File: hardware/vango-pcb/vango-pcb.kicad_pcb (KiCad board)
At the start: 2 copper layers, 70 x 66 mm, 13 parts, among them J1 XT60PW-M, J2 NeoPixel, J3 I2C, J4 Conn_01x07, J5 SPI, J6 Conn_01x02, SW1 SW_SPDT, U1 MD41B, U2 REG15D, U3 MD41B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

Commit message: update kicad pcb
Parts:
- moved SW1 10.9 mm to (94.7, 114.9)
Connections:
- J1 pad 1: Net-(J1-+) -> Net-(J1--)
- J1 pad 2: Net-(J1--) -> Net-(J1-+)
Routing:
- net Net-(J1-+): track 18.4 -> 8.88 mm, vias 1 -> 0
- net Net-(SW1-B): track 11.2 -> 17.2 mm, vias 0 -> 1
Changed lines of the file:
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@@
     (pad "" thru_hole rect (at 10.35 -6 270) (size 0.9 2) (drill oval 0.6 1.7) (layers "*.Cu" "*.Mask"))
     (pad "1" thru_hole roundrect (at 0 0 270) (size 4.1 4.1) (drill 2.7) (layers "*.Cu" "*.Mask") (roundrect_rratio 0.25)
-      (net 49 "Net-(J1-+)") (pinfunction "+") (pintype "passive"))
+      (net 41 "Net-(J1--)") (pinfunction "+") (pintype "passive"))
     (pad "2" thru_hole circle (at 7.2 0 270) (size 4.1 4.1) (drill 2.7) (layers "*.Cu" "*.Mask")
-      (net 41 "Net-(J1--)") (pinfunction "-") (pintype "passive"))
+      (net 49 "Net-(J1-+)") (pinfunction "-") (pintype "passive"))
     (pad "3" thru_hole rect (at 3.6 -3.65 270) (size 2.3 1.3) (drill oval 2 1) (layers "*.Cu" "*.Mask"))
     (model "${KICAD6_3DMODEL_DIR}/Connector_AMASS.3dshapes/AMASS_XT60IPW-M_1x03_P7.20mm_Horizontal.wrl"
@@
   )
   (footprint "Connector_PinHeader_2.54mm:PinHeader_1x03_P2.54mm_Vertical" (layer "F.Cu")
-    (at 83.82 114.3 90)
+    (at 94.662514 114.903264 90)
     (descr "Through hole straight pin header, 1x03, 2.54mm pitch, single row")
     (tags "Through hole pin header THT 1x03 2.54mm single row")
@@
   (segment (start 85.752474 76.807526) (end 83.82 78.74) (width 0.25) (layer "F.Cu") (net 35))
   (segment (start 97.127526 76.807526) (end 85.752474 76.807526) (width 0.25) (layer "F.Cu") (net 35))
-  (segment (start 86.36 114.3) (end 88.9 111.76) (width 0.25) (layer "B.Cu") (net 40))
-  (segment (start 88.9 106.68) (end 86.36 106.68) (width 0.25) (layer "B.Cu") (net 40))
-  (segment (start 88.9 111.76) (end 88.9 106.68) (width 0.25) (layer "B.Cu") (net 40))
+  (segment (start 86.36 106.68) (end 91.44 106.68) (width 0.25) (layer "F.Cu") (net 40))
+  (via (at 91.44 106.68) (size 0.8) (drill 0.4) (layers "F.Cu" "B.Cu") (net 40))
+  (segment (start 91.44 106.68) (end 91.44 111.76) (width 0.25) (layer "B.Cu") (net 40))
+  (segment (start 94.05925 111.76) (end 97.202514 114.903264) (width 0.25) (layer "B.Cu") (net 40))
+  (segment (start 91.44 111.76) (end 94.05925 111.76) (width 0.25) (layer "B.Cu") (net 40))
   (segment (start 92 104.14) (end 86.36 104.14) (width 0.25) (layer "F.Cu") (net 41))
-  (segment (start 95.6 107.74) (end 92 104.14) (width 0.25) (layer "F.Cu") (net 41))
+  (segment (start 95.6 100.54) (end 92 104.14) (width 0.25) (layer "F.Cu") (net 41))
   (segment (start 93.98 71.12) (end 99.06 71.12) (width 0.25) (layer "F.Cu") (net 44))
   (segment (start 81.28 63.5) (end 93.98 63.5) (width 0.25) (layer "F.Cu") (net 44))
@@
   (segment (start 86.36 55.88) (end 83.82 58.42) (width 0.25) (layer "F.Cu") (net 45))
   (segment (start 96.52 55.88) (end 86.36 55.88) (width 0.25) (layer "F.Cu") (net 45))
-  (segment (start 95.6 100.54) (end 92.5 100.54) (width 0.25) (layer "F.Cu") (net 49))
-  (segment (start 92.5 100.54) (end 91.44 101.6) (width 0.25) (layer "F.Cu") (net 49))
-  (via (at 91.44 101.6) (size 0.8) (drill 0.4) (layers "F.Cu" "B.Cu") (net 49))
-  (segment (start 91.44 111.76) (end 88.9 114.3) (width 0.25) (layer "B.Cu") (net 49))
-  (segment (start 91.44 101.6) (end 91.44 111.76) (width 0.25) (layer "B.Cu") (net 49))
+  (segment (start 95.6 110.76075) (end 99.742514 114.903264) (width 0.25) (layer "B.Cu") (net 49))
+  (segment (start 95.6 107.74) (end 95.6 110.76075) (width 0.25) (layer "B.Cu") (net 49))
   (zone (net 4) (net_name "GND") (layer "B.Cu") (hatch edge 0.5)
     (connect_pads (clearance 0.5))

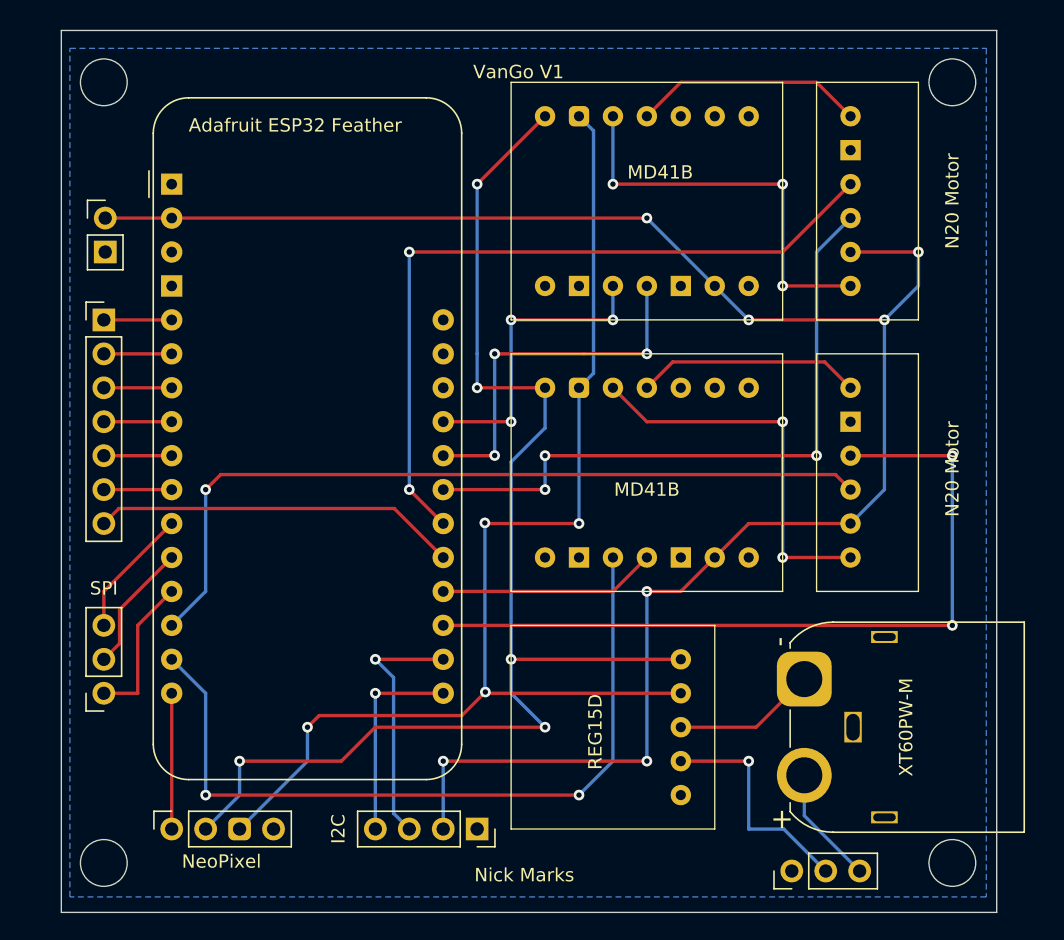
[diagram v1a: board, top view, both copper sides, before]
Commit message: add servo connector, more space for voltage reg
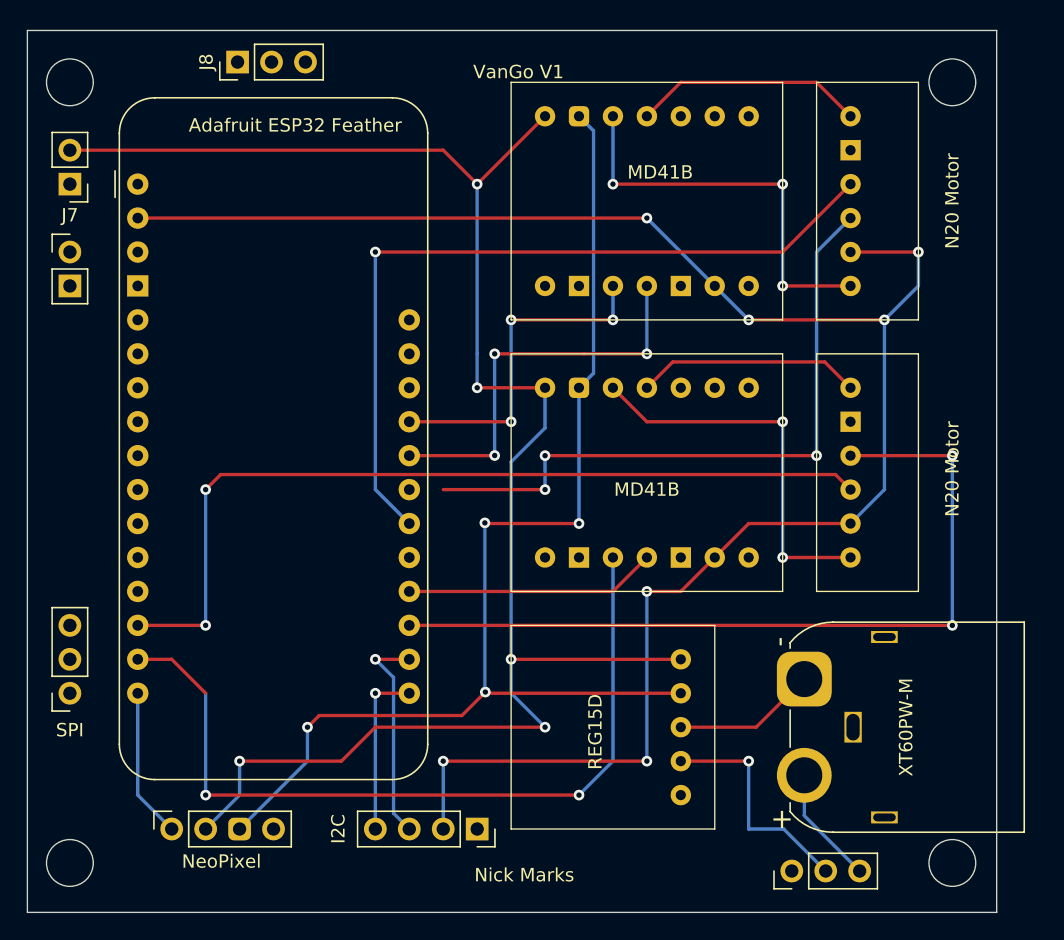
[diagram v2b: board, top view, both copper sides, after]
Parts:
- removed J4: Conn_01x07, Connector_PinHeader_2.54mm:PinHeader_1x07_P2.54mm_Vertical
- added J7: Conn_01x02, Connector_PinHeader_2.54mm:PinHeader_1x02_P2.54mm_Vertical, F.Cu at (40.6, 63.5)
- added J8: Servo, Connector_PinHeader_2.54mm:PinHeader_1x03_P2.54mm_Vertical, F.Cu at (53.2, 54.4)
- moved J6 3.67 mm to (40.6, 68.6)
- moved A1 2.54 mm to (45.7, 63.5)
- moved J5 2.54 mm to (40.6, 101.6)
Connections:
- J1 pad 1: Net-(J1--) -> Net-(J1-+)
- J1 pad 2: Net-(J1-+) -> Net-(J1--)
- J2 pad 3: GNDPWR -> GND
- U1 pad 9: GNDPWR -> GND
- U2 pad 4: GNDPWR -> GND
- U3 pad 9: GNDPWR -> GND
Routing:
- net GNDPWR: track 89.9 -> 0.00 mm, vias 4 -> 0
- net GND: track 0.00 -> 89.9 mm, vias 0 -> 4
- net +5V: track 97.8 -> 129.3 mm
- net /A8: track 27.4 -> 0.00 mm
- net /MISO: track 11.2 -> 0.00 mm
- net /MOSI: track 9.72 -> 0.00 mm
- net /SCK: track 9.72 -> 0.00 mm
- net /A5: track 5.08 -> 0.00 mm
- net /A4: track 5.08 -> 0.00 mm
- net /A3: track 5.08 -> 0.00 mm
- net /A2: track 5.08 -> 0.00 mm
- net /A1: track 5.08 -> 0.00 mm
- net /A0: track 5.08 -> 0.00 mm
- net /IO16: track 60.4 -> 64.4 mm, vias 1 -> 2
- net /IO33: track 56.5 -> 59.0 mm, vias 2 -> 1
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- removed copper zone on B.Cu, net GND
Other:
- board size 70 x 66 mm -> 72.5 x 66 mm

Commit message: pcb should be all good now
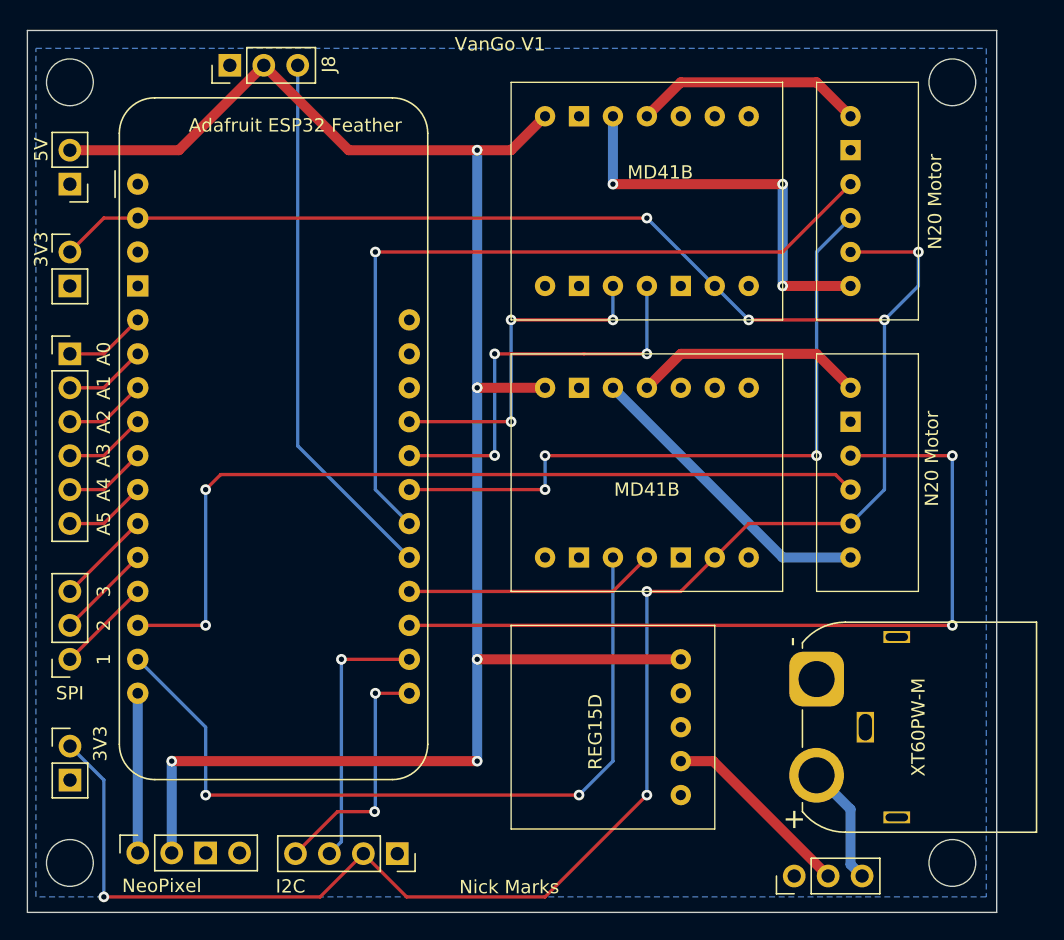
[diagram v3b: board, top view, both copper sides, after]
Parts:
- added 3V3: Conn_01x02, Connector_PinHeader_2.54mm:PinHeader_1x02_P2.54mm_Vertical, F.Cu at (40.7, 105.6)
- added J4: Conn_01x06, Connector_PinHeader_2.54mm:PinHeader_1x06_P2.54mm_Vertical, F.Cu at (40.6, 76.2)
- J8: value Servo -> SG90_Servo
- moved J3 6.25 mm to (65.1, 113.6)
- moved J2 3.11 mm to (45.7, 113.6)
- moved J5 2.54 mm to (40.6, 99.1)
- moved J1 0.92 mm to (96.5, 100.5)
- moved J8 0.63 mm to (52.6, 54.6)
- moved SW1 0.42 mm to (94.8, 115.3)
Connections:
- J1 pad 1: Net-(J1-+) -> GND
- J1 pad 2: Net-(J1--) -> Net-(J1-+)
- U2 pad 3: Net-(J1--) -> GND
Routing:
- net GND: track 89.9 -> 0.00 mm, vias 4 -> 0
- net +3V3: track 136.9 -> 184.1 mm
- net /A8: track 0.00 -> 40.3 mm
- net Net-(J1--): track 10.7 -> 0.00 mm
- net +5V: track 129.3 -> 137.6 mm
- net /SCK: track 0.00 -> 7.18 mm
- net /MOSI: track 0.00 -> 7.18 mm
- net /MISO: track 0.00 -> 7.18 mm
- net /A5: track 0.00 -> 6.13 mm
- net /A4: track 0.00 -> 6.13 mm
- net /A2: track 0.00 -> 6.13 mm
- net /A0: track 0.00 -> 6.13 mm
- net /A3: track 0.00 -> 6.13 mm
- net /A1: track 0.00 -> 6.13 mm
- net Net-(U1-OUT1): track 29.0 -> 23.0 mm, vias 2 -> 0
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- added copper zone on B.Cu, net GND
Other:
- board text added: "1"
- board text added: "2"
- board text added: "3"
- board text added: "3V3"
- board text added: "5V"
- board text added: "A0"
- board text added: "A1"
- board text added: "A2"
- board text added: "A3"
- board text added: "A4"
- board text added: "A5"

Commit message: change text to be "Vango V2"
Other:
- board text added: "VanGo V2"
- board text removed: "VanGo V1"
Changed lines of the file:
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@@
     (effects (font (size 1 1) (thickness 0.15)))
   )
-  (gr_text "VanGo V1\n" (at 69.432588 53.620954) (layer "F.SilkS")
+  (gr_text "VanGo V2\n" (at 69.432588 53.620954) (layer "F.SilkS")
     (effects (font (size 1 1) (thickness 0.15)) (justify left bottom))
   )

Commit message: move regulator over more, move servo pins
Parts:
- U4: value N20 Motor -> Left Motor
- U5: value N20 Motor -> Right Motor
- moved Servo 13.4 mm to (66.0, 54.6)
- moved U2 2.44 mm to (91.3, 104.1)
- renumbered J8 to Servo
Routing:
- net /A8: track 40.3 -> 45.9 mm
- net +5V: track 137.6 -> 142.3 mm
- net Net-(SW1-B): track 14.6 -> 12.2 mm
- net /IO27: vias 4 -> 3
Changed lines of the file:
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@@
   (net 48 "unconnected-(SW1-A-Pad1)")
   (footprint "vango_fplib:REG15D" (layer "F.Cu")
-    (at 88.9 104.14 90)
+    (at 91.34 104.14 90)
     (property "Sheetfile" "vango-pcb.kicad_sch")
     (property "Sheetname" "")
@@
         (effects (font (size 1 1) (thickness 0.1)))
     )
-    (fp_text value "MD41B" (at 8.498988 1.000226 unlocked) (layer "F.SilkS")
-        (effects (font (size 1 1) (thickness 0.15)))
-    )
-    (fp_text user "${REFERENCE}" (at 0 17.78 90 unlocked) (layer "F.Fab")
+    (fp_text value "MD41B" (at 6.890141 -0.022611 unlocked) (layer "F.SilkS")
+        (effects (font (size 1 1) (thickness 0.15)))
+    )
+    (fp_text user "${REFERENCE}" (at -2.54 2.54 90 unlocked) (layer "F.Fab")
         (effects (font (size 1 1) (thickness 0.15)))
     )
@@
         (effects (font (size 1 1) (thickness 0.1)))
     )
-    (fp_text value "N20 Motor" (at 6.325949 1.320008 90 unlocked) (layer "F.SilkS")
+    (fp_text value "Right Motor" (at 6.325949 1.320008 90 unlocked) (layer "F.SilkS")
         (effects (font (size 1 1) (thickness 0.15)))
     )
@@
         (effects (font (size 1 1) (thickness 0.1)))
     )
-    (fp_text value "N20 Motor" (at 6.087482 0.226007 90 unlocked) (layer "F.SilkS")
+    (fp_text value "Left Motor" (at 6.087482 0.226007 90 unlocked) (layer "F.SilkS")
         (effects (font (size 1 1) (thickness 0.15)))
     )
@@
         (effects (font (size 1 1) (thickness 0.1)))
     )
-    (fp_text value "MD41B" (at 5.08 0 unlocked) (layer "F.SilkS")
+    (fp_text value "MD41B" (at 6.603683 0.093009 unlocked) (layer "F.SilkS")
         (effects (font (size 1 1) (thickness 0.15)))
     )
@@
   )
   (footprint "Connector_PinHeader_2.54mm:PinHeader_1x03_P2.54mm_Vertical" (layer "F.Cu")
-    (at 52.609498 54.608195 90)
+    (at 66.04 54.608195 90)
     (descr "Through hole straight pin header, 1x03, 2.54mm pitch, single row")
     (tags "Through hole pin header THT 1x03 2.54mm single row")
@@
     (property "ki_keywords" "connector")
     (attr through_hole)
-    (fp_text reference "J8" (at 0.077974 7.412227 90) (layer "F.SilkS")
+    (fp_text reference "Servo" (at -0.106127 8.761665 180) (layer "F.SilkS")
         (effects (font (size 1 1) (thickness 0.15)))
     )
@@
     (effects (font (size 1 1) (thickness 0.15)))
   )
-  (gr_text "VanGo V2\n" (at 69.432588 53.620954) (layer "F.SilkS")
+  (gr_text "VanGo V2\n" (at 38.1 53.34) (layer "F.SilkS")
     (effects (font (size 1 1) (thickness 0.15)) (justify left bottom))
   )
@@
   (segment (start 83.82 91.44) (end 81.28 93.98) (width 0.25) (layer "F.Cu") (net 20))
   (segment (start 81.28 93.98) (end 66.04 93.98) (width 0.25) (layer "F.Cu") (net 20))
-  (segment (start 57.689498 54.608195) (end 57.689498 83.089498) (width 0.25) (layer "B.Cu") (net 21))
-  (segment (start 57.689498 83.089498) (end 66.04 91.44) (width 0.25) (layer "B.Cu") (net 21))
+  (segment (start 57.689498 83.089498) (end 66.04 91.44) (width 0.75) (layer "B.Cu") (net 21))
+  (segment (start 71.12 54.608195) (end 57.689498 68.038697) (width 0.75) (layer "B.Cu") (net 21))
+  (segment (start 57.689498 68.038697) (end 57.689498 83.089498) (width 0.75) (layer "B.Cu") (net 21))
   (segment (start 63.5 68.58) (end 93.98 68.58) (width 0.25) (layer "F.Cu") (net 22))
   (segment (start 93.98 68.58) (end 99.06 63.5) (width 0.25) (layer "F.Cu") (net 22))
@@
   (segment (start 63.5 86.36) (end 66.04 88.9) (width 0.25) (layer "B.Cu") (net 22))
   (segment (start 63.5 68.58) (end 63.5 86.36) (width 0.25) (layer "B.Cu") (net 22))
-  (segment (start 76.2 86.36) (end 66.04 86.36) (width 0.25) (layer "F.Cu") (net 23))
   (segment (start 96.52 83.82) (end 76.2 83.82) (width 0.25) (layer "F.Cu") (net 23))
-  (via (at 66.04 86.36) (size 0.8) (drill 0.4) (layers "F.Cu" "B.Cu") (net 23))
+  (segment (start 66.04 86.36) (end 76.2 86.36) (width 0.25) (layer "F.Cu") (net 23))
   (via (at 96.52 83.82) (size 0.8) (drill 0.4) (layers "F.Cu" "B.Cu") (net 23))
   (via (at 76.2 83.82) (size 0.8) (drill 0.4) (layers "F.Cu" "B.Cu") (net 23))
@@
   (segment (start 81.28 71.12) (end 81.28 73.66) (width 0.25) (layer "B.Cu") (net 25))
   (segment (start 73.66 73.66) (end 73.66 81.28) (width 0.25) (layer "B.Cu") (net 25))
+  (segment (start 68.58 58.42) (end 71.12 60.96) (width 0.75) (layer "F.Cu") (net 29))
+  (segment (start 68.58 54.608195) (end 62.228195 60.96) (width 0.75) (layer "F.Cu") (net 29))
   (segment (start 71.12 60.96) (end 73.66 60.96) (width 0.75) (layer "F.Cu") (net 29))
-  (segment (start 48.797693 60.96) (end 55.149498 54.608195) (width 0.75) (layer "F.Cu") (net 29))
+  (segment (start 88.8 99.06) (end 71.12 99.06) (width 0.75) (layer "F.Cu") (net 29))
   (segment (start 71.12 106.68) (end 48.26 106.68) (width 0.75) (layer "F.Cu") (net 29))
+  (segment (start 62.228195 60.96) (end 40.64 60.96) (width 0.75) (layer "F.Cu") (net 29))
   (segment (start 73.66 60.96) (end 76.2 58.42) (width 0.75) (layer "F.Cu") (net 29))
-  (segment (start 61.501303 60.96) (end 55.149498 54.608195) (width 0.75) (layer "F.Cu") (net 29))
-  (segment (start 40.64 60.96) (end 48.797693 60.96) (width 0.75) (layer "F.Cu") (net 29))
+  (segment (start 68.58 54.608195) (end 68.58 58.42) (width 0.75) (layer "F.Cu") (net 29))
   (segment (start 71.12 78.74) (end 76.2 78.74) (width 0.75) (layer "F.Cu") (net 29))
-  (segment (start 71.12 60.96) (end 61.501303 60.96) (width 0.75) (layer "F.Cu") (net 29))
-  (segment (start 86.36 99.06) (end 71.12 99.06) (width 0.75) (layer "F.Cu") (net 29))
   (via (at 71.12 99.06) (size 0.8) (drill 0.4) (layers "F.Cu" "B.Cu") (net 29))
   (via (at 71.12 78.74) (size 0.8) (drill 0.4) (layers "F.Cu" "B.Cu") (net 29))
@@
   (segment (start 86.36 76.2) (end 96.52 76.2) (width 0.75) (layer "F.Cu") (net 34))
   (segment (start 83.82 78.74) (end 86.36 76.2) (width 0.75) (layer "F.Cu") (net 34))
-  (segment (start 86.36 106.68) (end 88.788389 106.68) (width 0.75) (layer "F.Cu") (net 39))
-  (segment (start 88.788389 106.68) (end 97.385827 115.277438) (width 0.75) (layer "F.Cu") (net 39))
+  (segment (start 97.385827 115.277438) (end 88.8 106.691611) (width 0.75) (layer "F.Cu") (net 39))
+  (segment (start 88.8 106.691611) (end 88.8 106.68) (width 0.75) (layer "F.Cu") (net 39))
   (segment (start 81.28 63.5) (end 93.98 63.5) (width 0.75) (layer "F.Cu") (net 42))
   (segment (start 93.98 71.12) (end 99.06 71.12) (width 0.75) (layer "F.Cu") (net 42))
